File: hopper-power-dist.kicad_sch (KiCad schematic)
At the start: 37 parts, among them J1 XT60PW-M, J2 XT60PW-M, J5 XT60-F, J6 XT60PW-F, J7 XT60PW-F, J8 XT60PW-F, J9 XT60PW-F

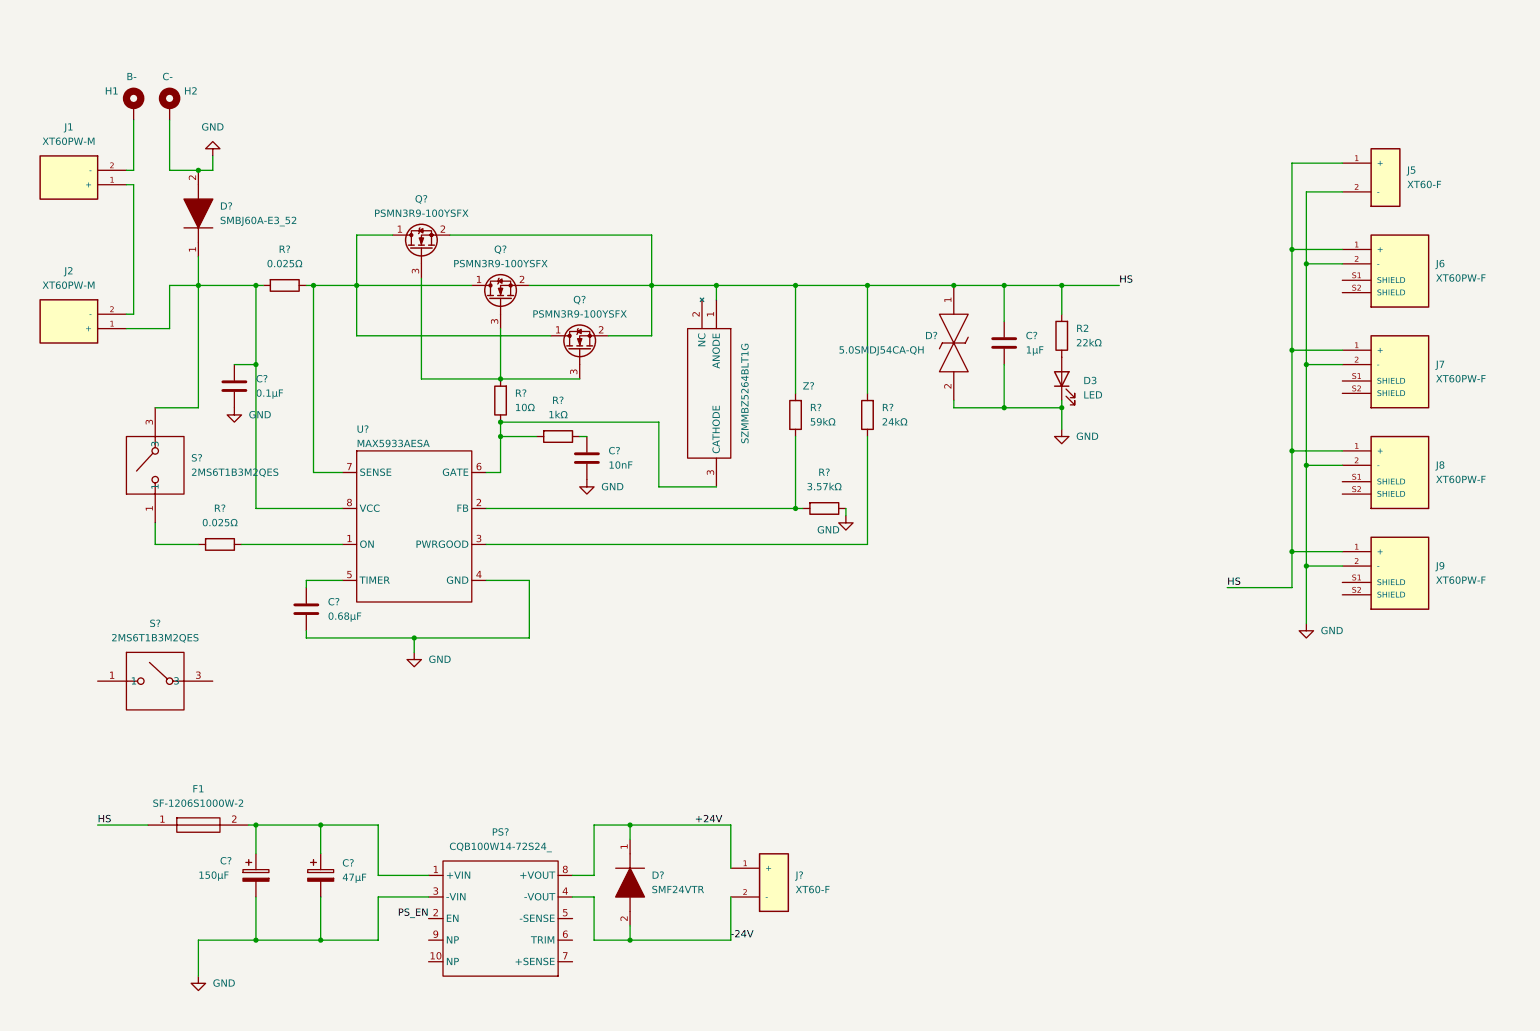
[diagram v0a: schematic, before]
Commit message: Add e-stop circuit
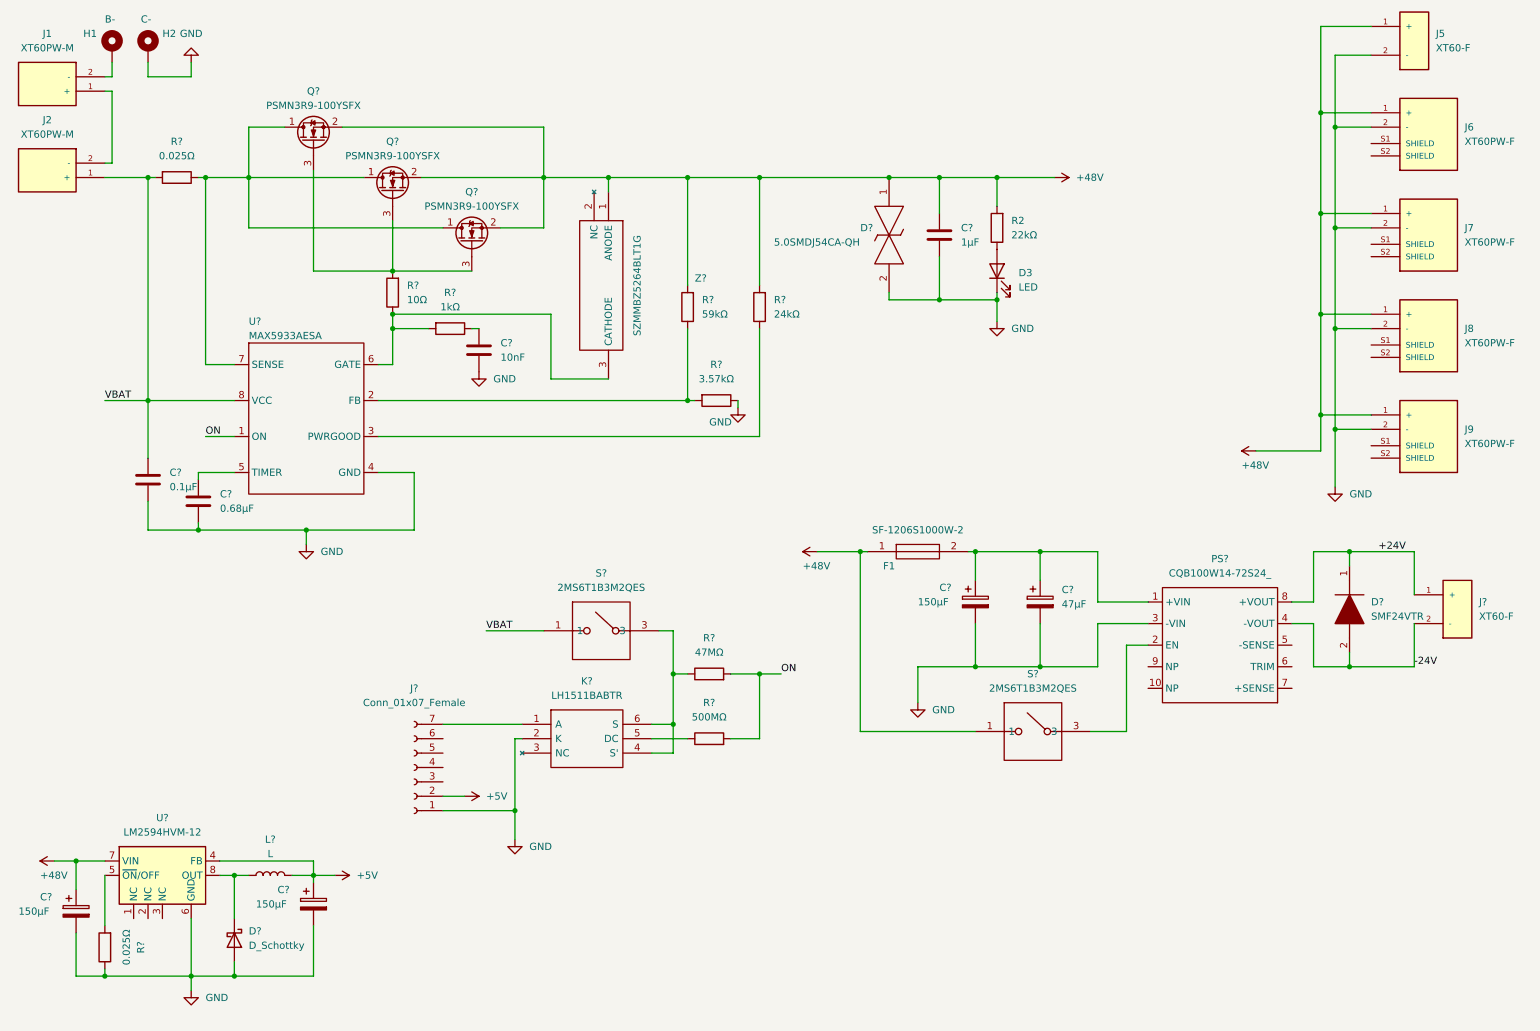
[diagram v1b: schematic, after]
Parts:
- removed D?: SMBJ60A-E3_52, DIOM5436X244N, symbol SamacSys_Parts:SMBJ60A-E3_52
- removed R?: 0.025Ω, Resistor_SMD:R_0603_1608Metric_Pad0.98x0.95mm_HandSolder, symbol Device:R
- removed S?: 2MS6T1B3M2QES, 2MS6T1B3M2QES, symbol 2ms6t1b3m2qes:2MS6T1B3M2QES
- added C? (x2): 150μF, symbol Device:C_Polarized
- added D?: D_Schottky, symbol Device:D_Schottky
- added J?: Conn_01x07_Female, symbol Connector:Conn_01x07_Female
- added K?: LH1511BABTR, SOP254P953X445-6N, symbol SamacSys_Parts:LH1511BABTR
- added L?: L, symbol Device:L
- added R?: 0.025Ω, Resistor_SMD:R_0603_1608Metric_Pad0.98x0.95mm_HandSolder, symbol Device:R
- added R?: 500MΩ, Resistor_SMD:R_0603_1608Metric_Pad0.98x0.95mm_HandSolder, symbol Device:R
- added R?: 47MΩ, Resistor_SMD:R_0603_1608Metric_Pad0.98x0.95mm_HandSolder, symbol Device:R
- added S?: 2MS6T1B3M2QES, 2MS6T1B3M2QES, symbol 2ms6t1b3m2qes:2MS6T1B3M2QES
- added U?: LM2594HVM-12, Package_SO:SOIC-8_3.9x4.9mm_P1.27mm, symbol Regulator_Switching:LM2594HVM-12
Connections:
- net HS is gone; now on net +48V: C?.1, D?.1, F1.1, J5.1 (+), J6.1 (+), J7.1 (+), J8.1 (+), J9.1 (+), Q?.2 (S), Q?.2 (S), Q?.2 (S), R2.2, R?.2, R?.2, Z?.1 (ANODE)
- net PS_EN is gone; now on an unnamed net: PS?.2 (EN)
- net GND: now also C?.2, C?.2, D?.2 (A), J?.1 (Pin_1), K?.2 (K), R?.1, U?.6 (GND)
- net VBAT: now reaches C?.1, J2.1 (+), R?.2, U?.8 (VCC)
- net VBAT: now also S?.1
- net +48V: now reaches S?.1
- net +48V: now also C?.1, U?.7 (VIN)
- net ON: now reaches U?.1 (ON)
- net ON: now also R?.2, R?.2
- new net: R?.2, U?.5 (~{ON}/OFF)
- new net: K?.4 (S'), K?.6 (S), R?.1, S?.3
- new net: J?.7 (Pin_7), K?.1 (A)
- new net: K?.5 (DC), R?.1
- new net: D?.1 (K), L?.1, U?.8 (OUT)
- new net +5V: C?.1, J?.2 (Pin_2), L?.2, U?.4 (FB)
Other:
- moved on the sheet: C?, D3, D?, F1, H1, H2, J1, J2, J5, J6, J7, J8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

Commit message: Change estop circuit to 5V
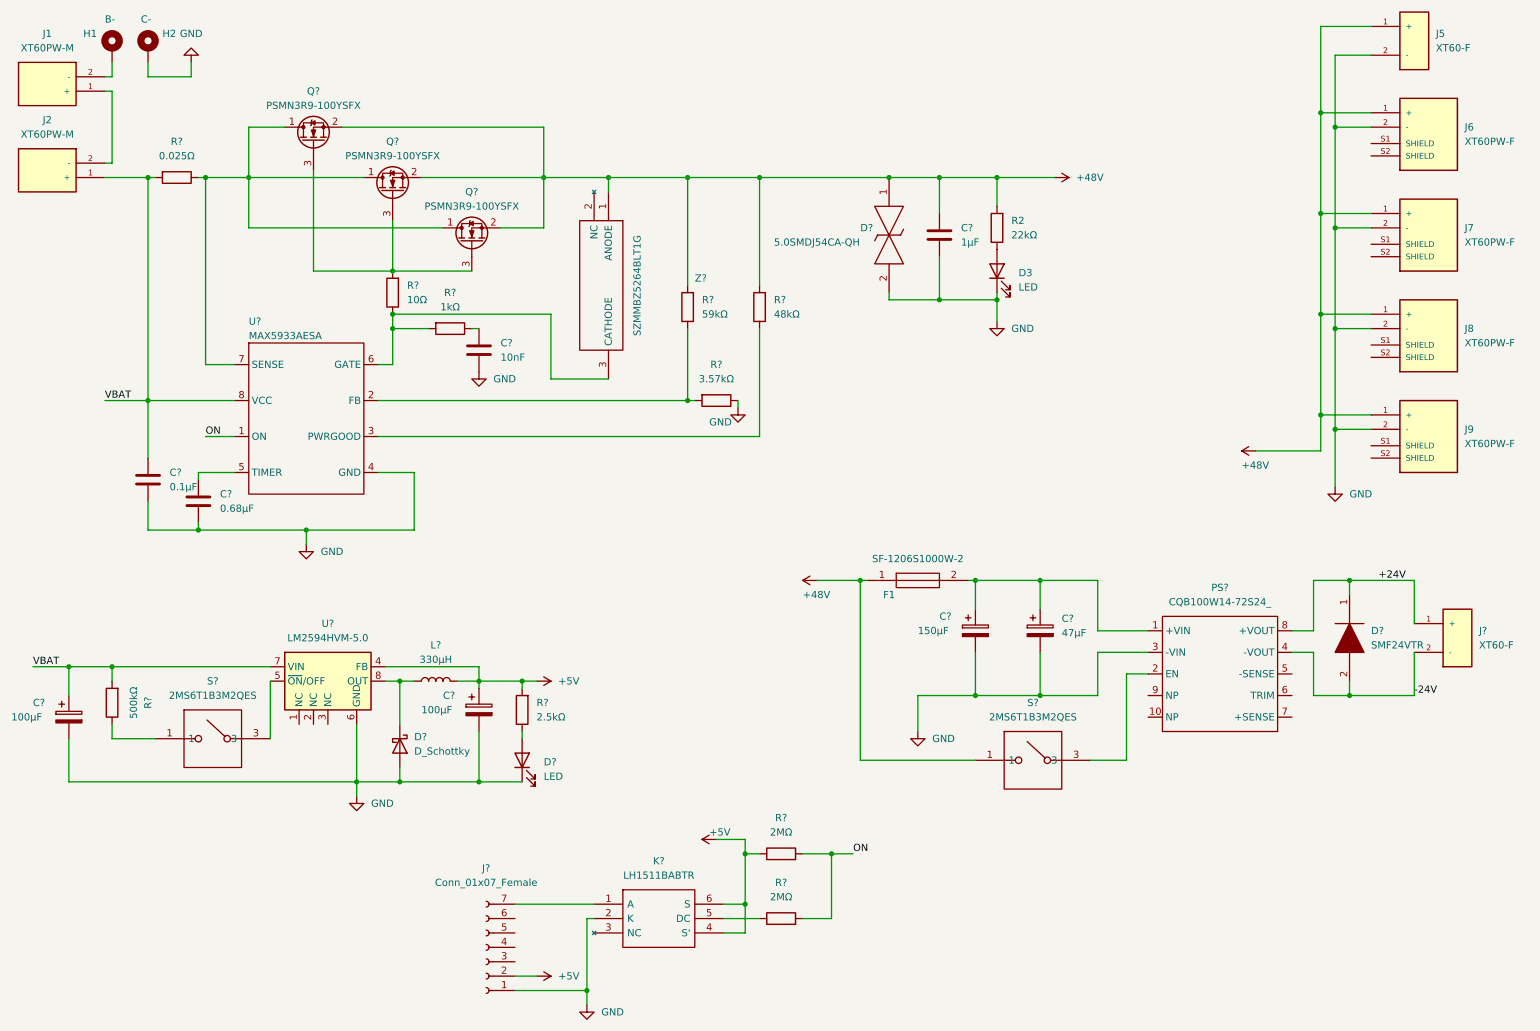
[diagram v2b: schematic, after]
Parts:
- removed R?: 0.025Ω, Resistor_SMD:R_0603_1608Metric_Pad0.98x0.95mm_HandSolder, symbol Device:R
- removed S?: 2MS6T1B3M2QES, 2MS6T1B3M2QES, symbol 2ms6t1b3m2qes:2MS6T1B3M2QES
- removed U?: LM2594HVM-12, Package_SO:SOIC-8_3.9x4.9mm_P1.27mm, symbol Regulator_Switching:LM2594HVM-12
- added D?: LED, LED_SMD:LED_0603_1608Metric, symbol Device:LED
- added R?: 2.5kΩ, Resistor_SMD:R_0603_1608Metric_Pad0.98x0.95mm_HandSolder, symbol Device:R
- added R?: 500kΩ, Resistor_SMD:R_0603_1608Metric_Pad0.98x0.95mm_HandSolder, symbol Device:R
- added S?: 2MS6T1B3M2QES, 2MS6T1B3M2QES, symbol 2ms6t1b3m2qes:2MS6T1B3M2QES
- added U?: LM2594HVM-5.0, Package_SO:SOIC-8_3.9x4.9mm_P1.27mm, symbol Regulator_Switching:LM2594HVM-5.0
- C? (x2): value 150μF -> 100μF
- L?: value L -> 330μH
- R?: value 24kΩ -> 48kΩ
- R?: value 500MΩ -> 2MΩ
- R?: value 47MΩ -> 2MΩ
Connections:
- net +48V: no longer C?.1
- net +5V: now also K?.4 (S'), K?.6 (S), R?.1, R?.2, U?.4 (FB)
- net GND: now also D?.1 (K), U?.6 (GND)
- net VBAT: now also C?.1, R?.2, U?.7 (VIN)
- net at D?.1 (K), L?.1: now also U?.8 (OUT)
- new net: R?.1, S?.1
- new net: S?.3, U?.5 (~{ON}/OFF)
- new net: D?.2 (A), R?.1
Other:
- moved on the sheet: C?, D?, F1, J?, K?, L?, PS?, R?, S?
